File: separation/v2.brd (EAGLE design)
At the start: 40.6 x 27.9 mm, 18 parts, among them Q1 IRLZ24NPBF

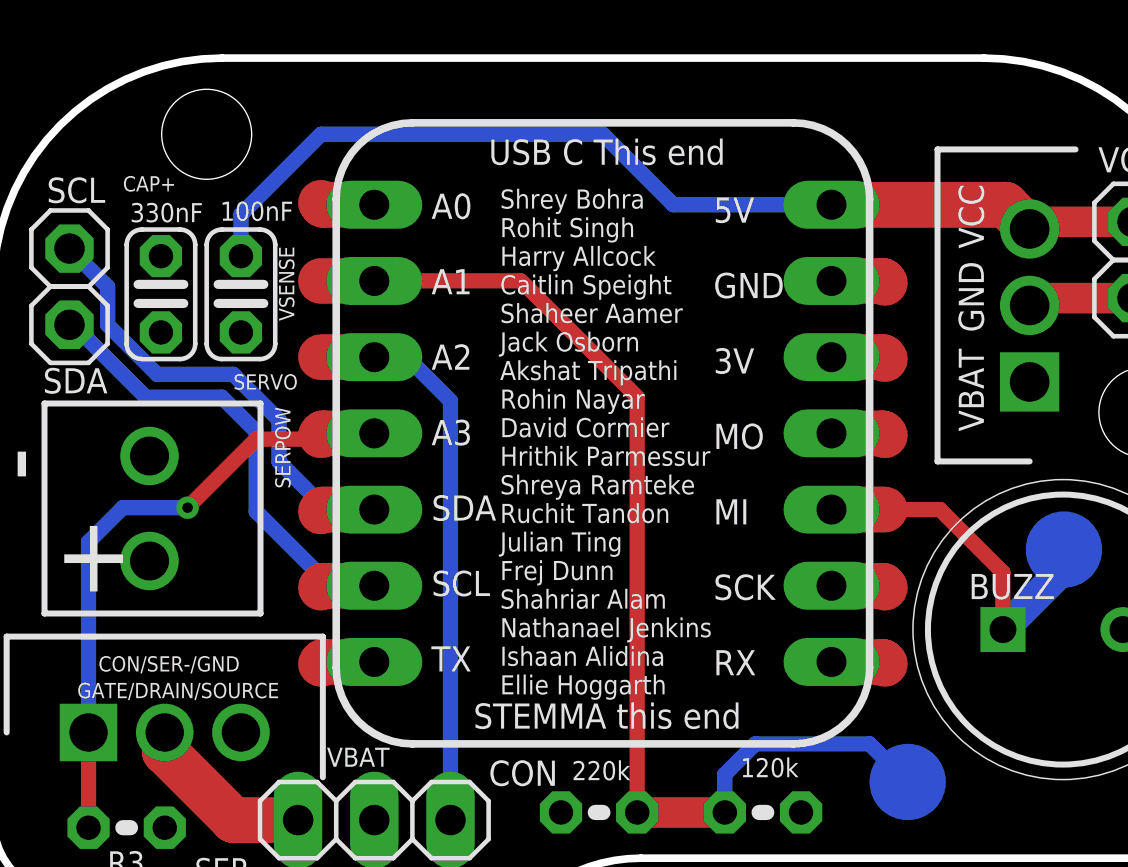
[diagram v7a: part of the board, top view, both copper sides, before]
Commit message: remove extra solder pad area
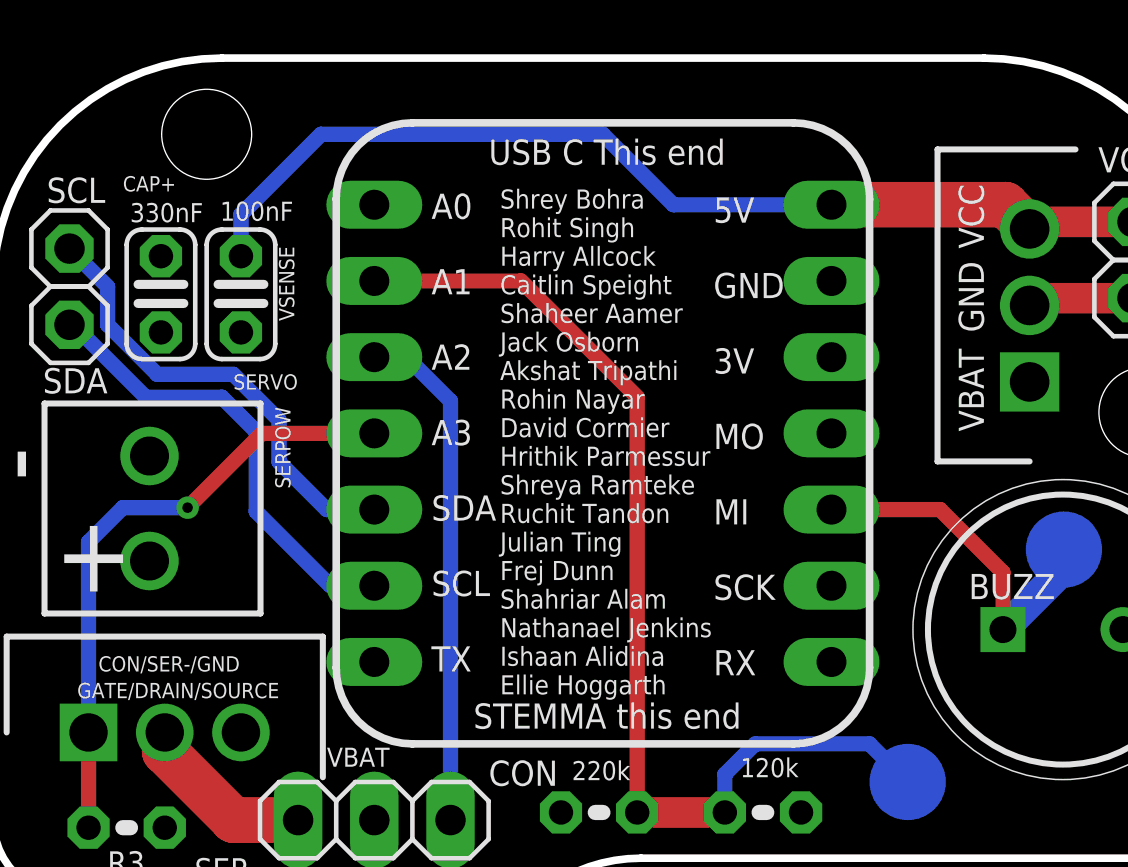
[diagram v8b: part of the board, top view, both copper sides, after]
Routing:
- net SDA: track 17.1 -> 15.3 mm
- net A0: track 1.80 -> 0.00 mm
- net GND: track 5.33 -> 3.53 mm
- net TX: track 1.80 -> 0.00 mm
- net SCK: track 1.80 -> 0.00 mm
- net RX: track 1.80 -> 0.00 mm
- net MOSI: track 1.80 -> 0.00 mm
- net +3V3: track 1.80 -> 0.00 mm
- net SERPOW: track 22.4 -> 20.5 mm
- net SCL: track 17.1 -> 15.3 mm
- net VSENSE: track 37.2 -> 35.4 mm
- net SERVO: track 18.9 -> 17.1 mm
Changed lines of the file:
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@@
 <layer number="27" name="tValues" color="7" fill="1" visible="yes" active="yes"/>
 <layer number="28" name="bValues" color="7" fill="1" visible="yes" active="yes"/>
-<layer number="29" name="tStop" color="7" fill="3" visible="no" active="yes"/>
+<layer number="29" name="tStop" color="7" fill="3" visible="yes" active="yes"/>
 <layer number="30" name="bStop" color="7" fill="6" visible="yes" active="yes"/>
 <layer number="31" name="tCream" color="7" fill="4" visible="no" active="yes"/>
@@
 <wire x1="6.35" y1="23.241" x2="8.89" y2="20.701" width="0.254" layer="21" curve="-90"/>
 <text x="64.4398" y="16.5608" size="1.016" layer="21" font="vector" ratio="12" rot="R180" align="center"></text>
-<wire x1="-7.62" y1="20.574" x2="-9.398" y2="20.574" width="1.524" layer="29"/>
-<wire x1="-7.62" y1="17.907" x2="-9.398" y2="17.907" width="1.524" layer="29"/>
 <wire x1="-7.62" y1="15.367" x2="-7.747" y2="15.494" width="1.524" layer="29"/>
 <wire x1="-7.62" y1="10.414" x2="-7.747" y2="10.287" width="1.524" layer="29"/>
-<wire x1="-7.747" y1="10.287" x2="-9.398" y2="10.287" width="1.524" layer="29"/>
-<wire x1="-7.62" y1="15.367" x2="-9.398" y2="15.367" width="1.524" layer="29"/>
-<wire x1="-7.62" y1="12.827" x2="-9.398" y2="12.827" width="1.524" layer="29"/>
-<wire x1="-7.62" y1="7.747" x2="-9.398" y2="7.747" width="1.524" layer="29"/>
-<wire x1="-7.62" y1="5.207" x2="-9.398" y2="5.207" width="1.524" layer="29"/>
-<wire x1="7.62" y1="20.447" x2="9.398" y2="20.447" width="1.524" layer="29"/>
-<wire x1="7.62" y1="17.907" x2="9.398" y2="17.907" width="1.524" layer="29"/>
-<wire x1="7.62" y1="15.367" x2="9.398" y2="15.367" width="1.524" layer="29"/>
-<wire x1="7.62" y1="12.827" x2="9.398" y2="12.827" width="1.524" layer="29"/>
-<wire x1="7.62" y1="10.287" x2="9.398" y2="10.287" width="1.524" layer="29"/>
-<wire x1="7.62" y1="7.747" x2="9.398" y2="7.747" width="1.524" layer="29"/>
-<wire x1="7.62" y1="5.207" x2="9.398" y2="5.207" width="1.524" layer="29"/>
 <hole x="-13.208" y="22.86" drill="3"/>
 <hole x="18.034" y="13.589" drill="3"/>
@@
 <contactref element="LOUD" pad="2"/>
 <contactref element="R2" pad="2"/>
-<wire x1="7.62" y1="17.9705" x2="9.3345" y2="17.9705" width="1.524" layer="1"/>
-<wire x1="9.3345" y1="17.9705" x2="9.398" y2="17.907" width="1.524" layer="1"/>
 <contactref element="LDO" pad="2"/>
 <contactref element="JP1" pad="1"/>
@@
 <signal name="MOSI">
 <contactref element="MCU-R" pad="4"/>
-<wire x1="7.62" y1="12.8905" x2="9.3345" y2="12.8905" width="1.524" layer="1"/>
-<wire x1="9.3345" y1="12.8905" x2="9.398" y2="12.827" width="1.524" layer="1"/>
 </signal>
 <signal name="SCK">
 <contactref element="MCU-R" pad="2"/>
-<wire x1="7.62" y1="7.8105" x2="9.3345" y2="7.8105" width="1.524" layer="1"/>
-<wire x1="9.3345" y1="7.8105" x2="9.398" y2="7.747" width="1.524" layer="1"/>
 </signal>
 <signal name="SDA">
 <contactref element="MCU-L" pad="5"/>
-<wire x1="-7.62" y1="10.3505" x2="-9.3345" y2="10.3505" width="1.524" layer="1"/>
-<wire x1="-9.3345" y1="10.3505" x2="-9.398" y2="10.287" width="1.524" layer="1"/>
 <contactref element="JP2" pad="1"/>
 <wire x1="-17.78" y1="19.05" x2="-16.51" y2="17.78" width="0.508" layer="16"/>
@@
 <signal name="SCL">
 <contactref element="MCU-L" pad="6"/>
-<wire x1="-7.62" y1="7.8105" x2="-9.3345" y2="7.8105" width="1.524" layer="1"/>
-<wire x1="-9.3345" y1="7.8105" x2="-9.398" y2="7.747" width="1.524" layer="1"/>
 <contactref element="JP3" pad="1"/>
 <wire x1="-7.62" y1="7.8105" x2="-9.0805" y2="7.8105" width="0.508" layer="16"/>
@@
 <signal name="+3V3">
 <contactref element="MCU-R" pad="5"/>
-<wire x1="7.62" y1="15.4305" x2="9.3345" y2="15.4305" width="1.524" layer="1"/>
-<wire x1="9.3345" y1="15.4305" x2="9.398" y2="15.367" width="1.524" layer="1"/>
 </signal>
 <signal name="PB22/I6/SERCOM5.3">
@@
 <signal name="TX">
 <contactref element="MCU-L" pad="7"/>
-<wire x1="-7.62" y1="5.2705" x2="-9.3345" y2="5.2705" width="1.524" layer="1"/>
-<wire x1="-9.3345" y1="5.2705" x2="-9.398" y2="5.207" width="1.524" layer="1"/>
 </signal>
 <signal name="RX">
 <contactref element="MCU-R" pad="1"/>
-<wire x1="7.62" y1="5.2705" x2="9.3345" y2="5.2705" width="1.524" layer="1"/>
-<wire x1="9.3345" y1="5.2705" x2="9.398" y2="5.207" width="1.524" layer="1"/>
 </signal>
 <signal name="VBAT">
@@
 <contactref element="SERCON" pad="3"/>
 <contactref element="MCU-L" pad="3"/>
-<wire x1="-7.62" y1="15.4305" x2="-9.398" y2="15.4305" width="1.524" layer="1"/>
 <wire x1="-7.62" y1="15.4305" x2="-6.5405" y2="15.4305" width="0.508" layer="16"/>
 <wire x1="-6.5405" y1="15.4305" x2="-5.08" y2="13.97" width="0.508" layer="16"/>
@@
 <contactref element="MCU-R" pad="3"/>
 <wire x1="13.335" y1="6.35" x2="13.335" y2="8.255" width="0.508" layer="1"/>
-<wire x1="11.2395" y1="10.3505" x2="9.398" y2="10.3505" width="0.508" layer="1"/>
 <wire x1="13.335" y1="8.255" x2="11.2395" y2="10.3505" width="0.508" layer="1"/>
-<wire x1="7.62" y1="10.3505" x2="9.398" y2="10.3505" width="1.524" layer="1"/>
 <contactref element="TP6" pad="TP"/>
 <wire x1="15.367" y1="9.017" x2="15.367" y2="8.89" width="0.254" layer="16"/>
 <wire x1="13.335" y1="6.35" x2="15.367" y2="8.382" width="1.016" layer="16"/>
 <wire x1="15.367" y1="8.382" x2="15.367" y2="8.89" width="1.016" layer="16"/>
+<wire x1="11.2395" y1="10.3505" x2="7.62" y2="10.3505" width="0.508" layer="1"/>
 </signal>
 <signal name="VSENSE">
@@
 <contactref element="R2" pad="1"/>
 <contactref element="MCU-L" pad="2"/>
-<wire x1="-7.62" y1="17.9705" x2="-9.398" y2="17.9705" width="1.524" layer="1"/>
 <contactref element="TP2" pad="TP"/>
 <wire x1="1.143" y1="0.254" x2="4.064" y2="0.254" width="1.016" layer="1"/>
@@
 <signal name="A0">
 <contactref element="MCU-L" pad="1"/>
-<wire x1="-7.62" y1="20.5105" x2="-9.3345" y2="20.5105" width="1.524" layer="1"/>
-<wire x1="-9.3345" y1="20.5105" x2="-9.398" y2="20.574" width="1.524" layer="1"/>
 </signal>
 <signal name="SER-" class="1">
@@
 <signal name="SERPOW">
 <contactref element="MCU-L" pad="4"/>
-<wire x1="-7.62" y1="12.8905" x2="-9.3345" y2="12.8905" width="1.524" layer="1"/>
-<wire x1="-9.3345" y1="12.8905" x2="-9.398" y2="12.827" width="1.524" layer="1"/>
 <contactref element="Q1" pad="1"/>
 <contactref element="R3" pad="1"/>
 <wire x1="-17.145" y1="2.921" x2="-17.145" y2="-0.254" width="0.508" layer="1"/>
-<wire x1="-7.62" y1="12.8905" x2="-7.8105" y2="12.7" width="0.508" layer="1"/>
-<wire x1="-11.557" y1="12.7" x2="-13.843" y2="10.414" width="0.508" layer="1"/>
 <via x="-13.843" y="10.414" extent="1-16" drill="0.35"/>
 <wire x1="-13.843" y1="10.414" x2="-16.002" y2="10.414" width="0.508" layer="16"/>
 <wire x1="-16.002" y1="10.414" x2="-17.145" y2="9.271" width="0.508" layer="16"/>
 <wire x1="-17.145" y1="9.271" x2="-17.145" y2="2.921" width="0.508" layer="16"/>
-<wire x1="-7.8105" y1="12.7" x2="-11.557" y2="12.7" width="0.508" layer="1"/>
+<wire x1="-11.3665" y1="12.8905" x2="-7.62" y2="12.8905" width="0.508" layer="1"/>
+<wire x1="-13.843" y1="10.414" x2="-11.3665" y2="12.8905" width="0.508" layer="1"/>
 </signal>
 </signals>
@@
 <mfgpreviewcolor name="substratecolor" color="0xFF786E46"/>
 </mfgpreviewcolors>
-<errors>
-</errors>
 </board>
 </drawing>
